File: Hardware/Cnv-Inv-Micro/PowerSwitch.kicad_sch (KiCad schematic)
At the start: 4 parts, among them Q13 SS8050, Q14 SS8550, Q15 IRFB4110PBF

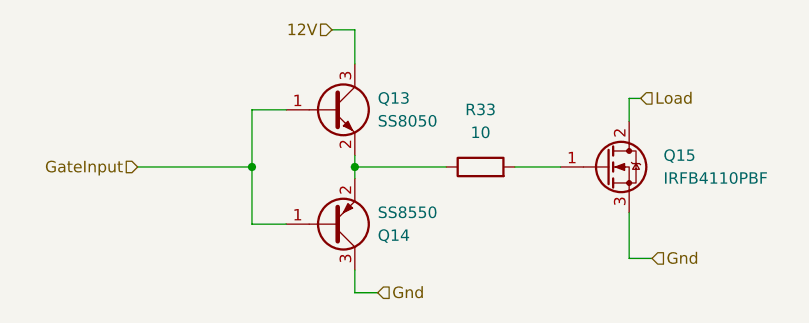
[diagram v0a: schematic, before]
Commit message: Avances en PCB conversor y inversor - Simulaciones de modulacion
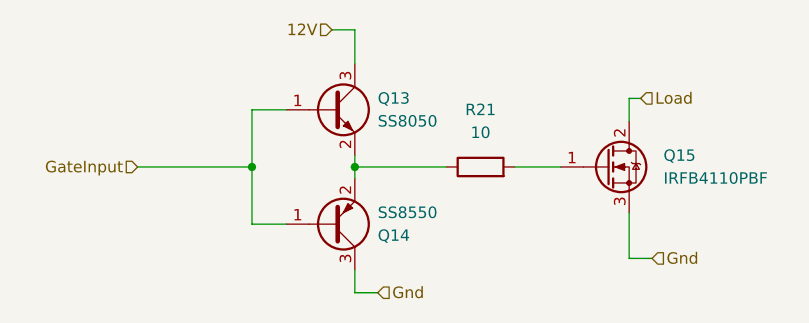
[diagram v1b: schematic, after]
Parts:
- renumbered R33 to R21
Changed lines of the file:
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@@
 		(dnp no)
 		(fields_autoplaced yes)
-		(property "Reference" "R33"
+		(property "Reference" "R21"
 			(at 143.51 62.23 90)
 			(effects
@@
 			(project "VFD_V1"
 				(path "/e60c11d9-ab9e-4760-a4a7-008fcec65a72/c6551446-5e26-4d9a-a5bc-1c867d865e21/114be0da-6ec0-43cc-95ec-fead423de7f2/285d2753-215f-428f-a3e3-1ef4b695e2d7"
-					(reference "R35")
+					(reference "R23")
 					(unit 1)
 				)
 				(path "/e60c11d9-ab9e-4760-a4a7-008fcec65a72/c6551446-5e26-4d9a-a5bc-1c867d865e21/114be0da-6ec0-43cc-95ec-fead423de7f2/b376caf9-3098-44f3-80b6-fb87206c02dc"
-					(reference "R33")
+					(reference "R21")
 					(unit 1)
 				)
 				(path "/e60c11d9-ab9e-4760-a4a7-008fcec65a72/c6551446-5e26-4d9a-a5bc-1c867d865e21/4ead1ef3-6642-476a-91a4-2f6f295e53fc/285d2753-215f-428f-a3e3-1ef4b695e2d7"
-					(reference "R38")
+					(reference "R26")
 					(unit 1)
 				)
 				(path "/e60c11d9-ab9e-4760-a4a7-008fcec65a72/c6551446-5e26-4d9a-a5bc-1c867d865e21/4ead1ef3-6642-476a-91a4-2f6f295e53fc/b376caf9-3098-44f3-80b6-fb87206c02dc"
-					(reference "R37")
+					(reference "R25")
 					(unit 1)
 				)
